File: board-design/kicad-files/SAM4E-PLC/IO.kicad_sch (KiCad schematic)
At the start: 138 parts, among them Q10 BC807, Q11 BC807, Q12 BC807, Q3 BC807, Q4 BC807, Q5 BC807, Q6 BC807, Q7 BC807, Q8 BC807, Q9 BC807, U11 ULN2803CDWR, U12 74AC14SCX, U13 SN74HC240DBR

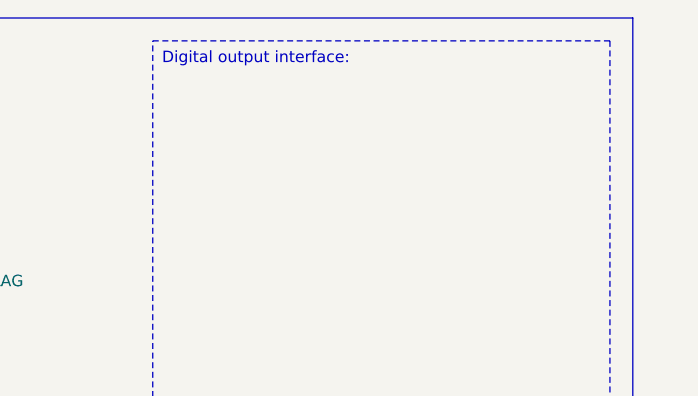
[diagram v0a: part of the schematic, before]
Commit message: [FIX]
Updated footprints for tactile switches.

Signed-off-by: Nicolae-Andrei Vasile <vasilenicolaeandrei@gmail.com>
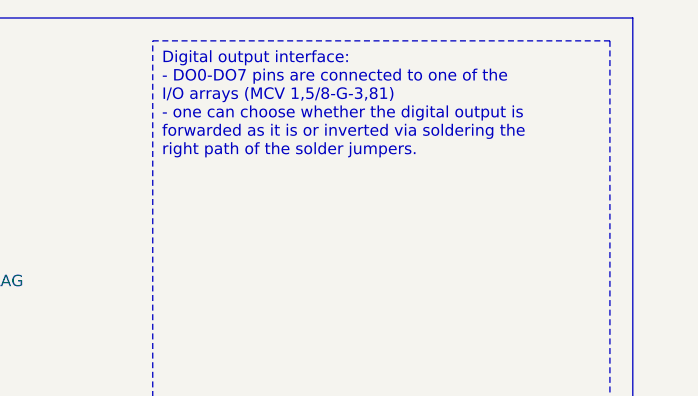
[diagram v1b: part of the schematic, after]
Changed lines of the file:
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@@
     (fill (type none))
   )
-  (text_box "Digital output interface:\n"
+  (text_box "Digital output interface:\n- DO0-DO7 pins are connected to one of the I/O arrays (MCV 1,5/8-G-3,81)\n- one can choose whether the digital output is forwarded as it is or inverted via soldering the right path of the solder jumpers."
     (at 349.25 20.32 0) (size 50.8 40.64)
     (stroke (width 0) (type dash) (color 255 0 0 1))

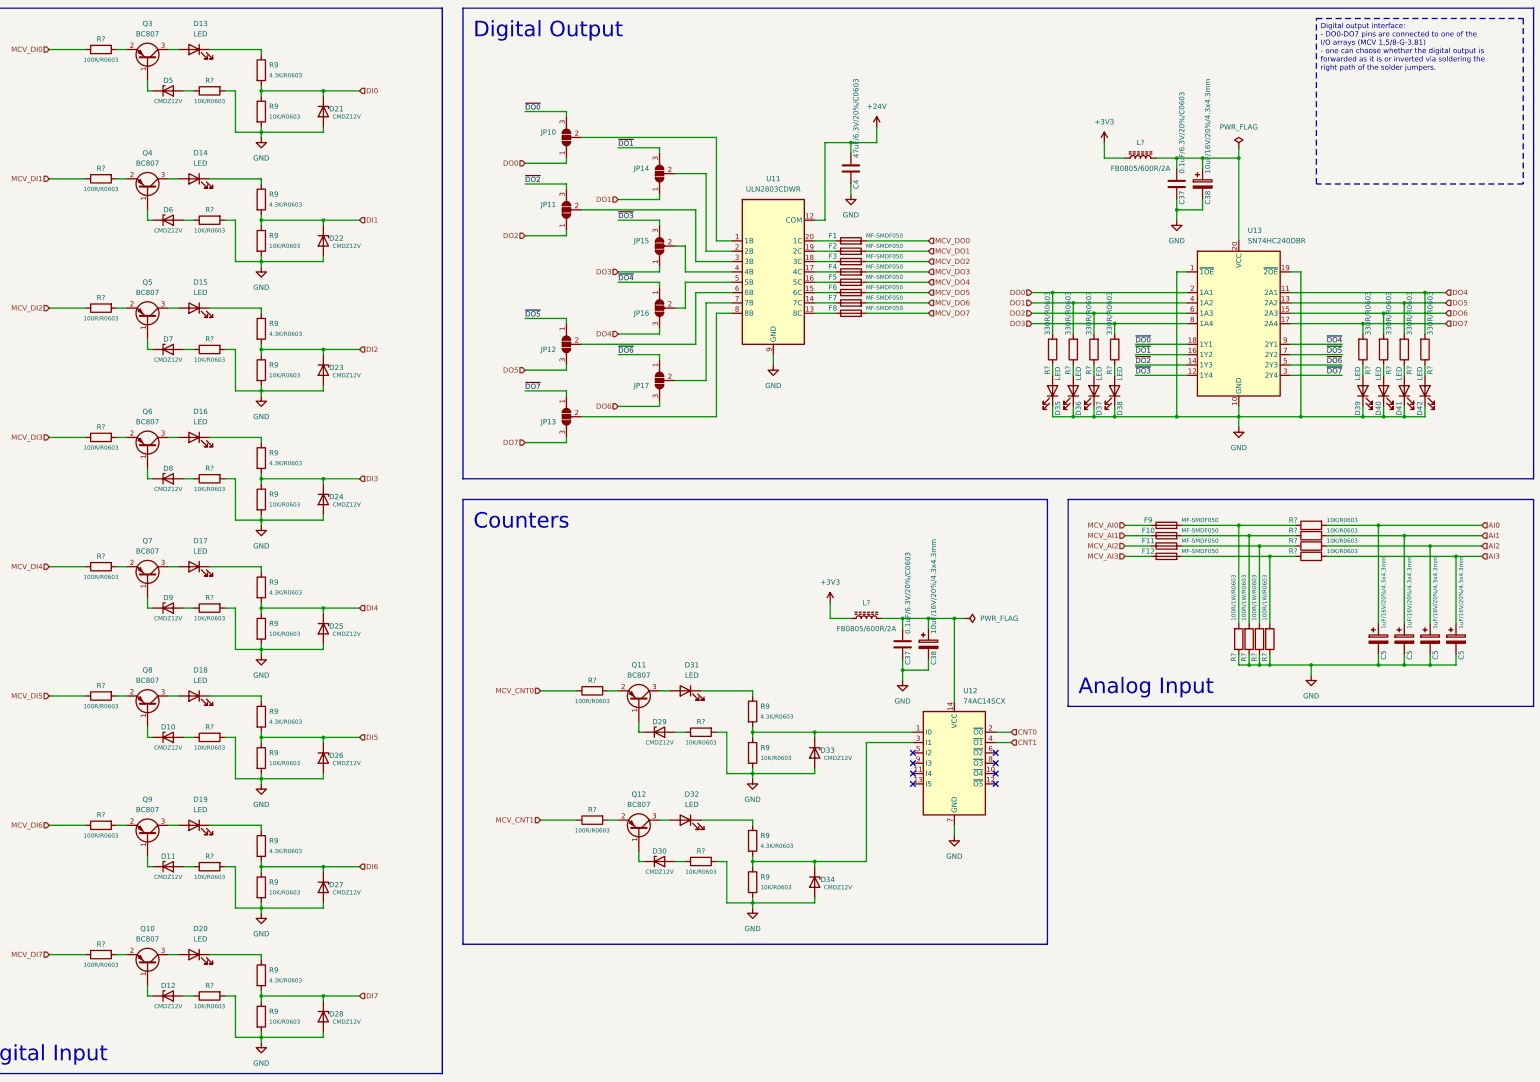
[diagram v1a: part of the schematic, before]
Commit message: [UPDATE]
Refactored schematic for LTE, Power and other schematic sub-sheets.

Signed-off-by: Nicolae-Andrei Vasile <vasilenicolaeandrei@gmail.com>
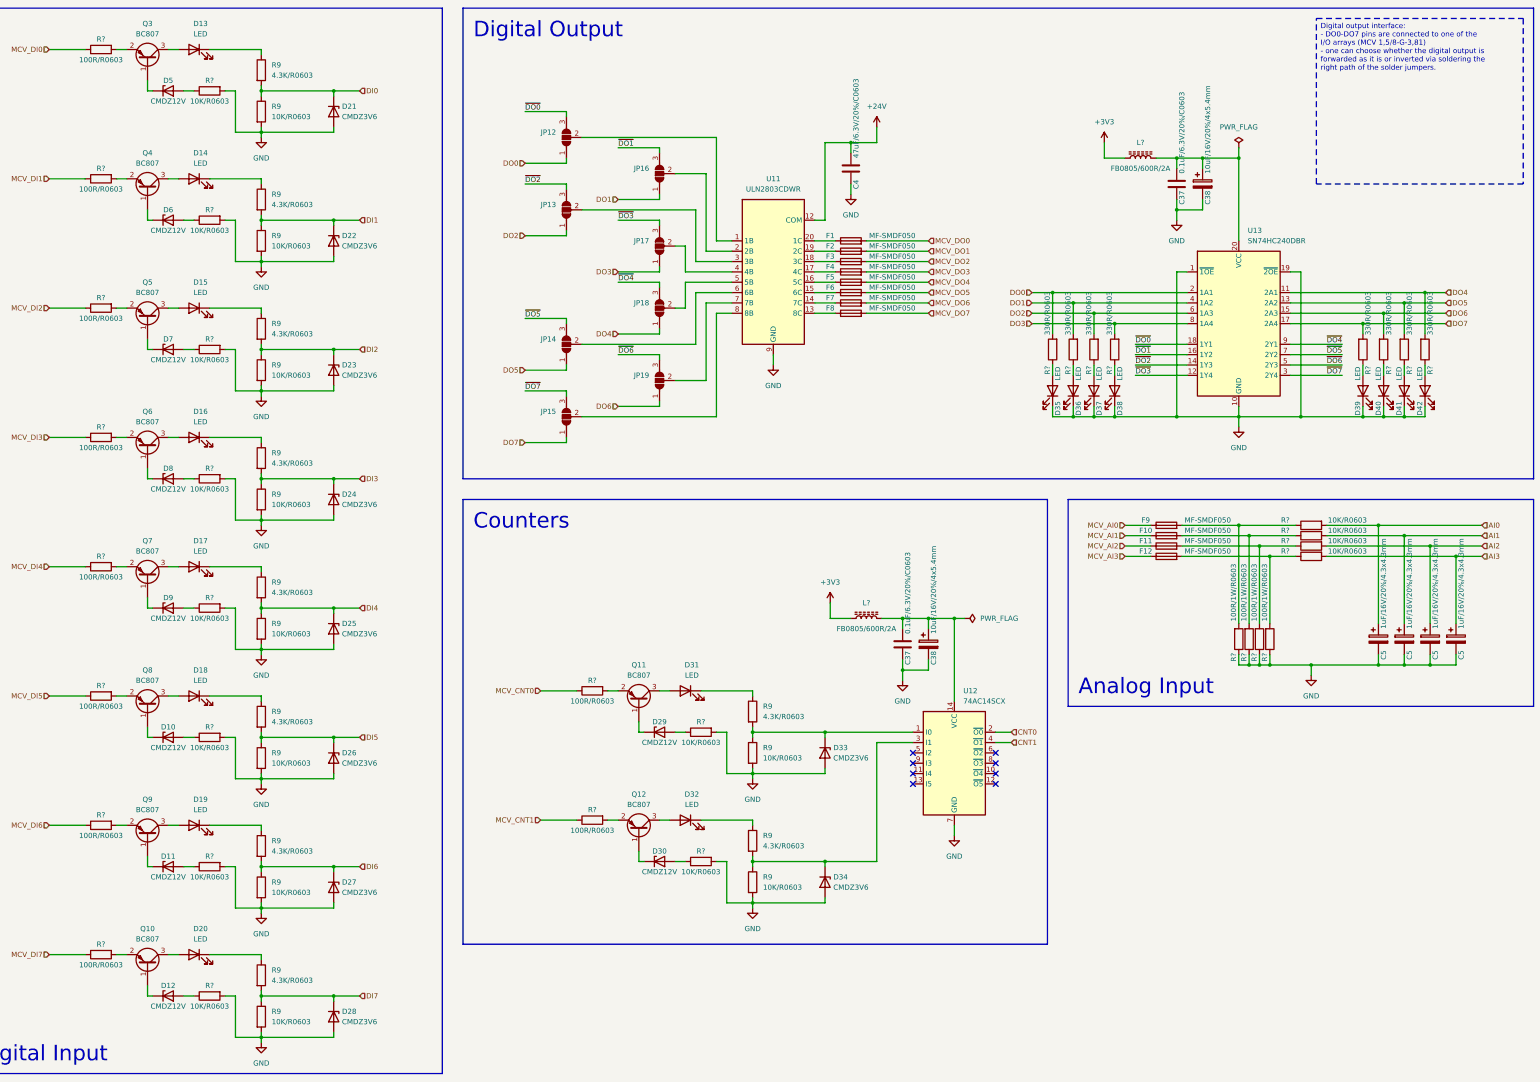
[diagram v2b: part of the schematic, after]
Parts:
- removed C5 (x3): 1uF/16V/20%/4.3x4.3mm, symbol Device:C_Polarized
- removed JP11, JP12: SolderJumper_3_Open, symbol Jumper:SolderJumper_3_Open
- removed L?: FB0805/600R/2A, symbol Device:L_Ferrite
- removed R9 (x9): 10K/R0603, symbol Device:R
- removed R9 (x9): 4.3K/R0603, symbol Device:R
- removed R? (x3): 100R/1W/R0603, Resistor_SMD:R_0603_1608Metric, symbol Device:R
- removed R? (x9): 100R/R0603, Resistor_SMD:R_0603_1608Metric, symbol Device:R
- removed R? (x12): 10K/R0603, Resistor_SMD:R_0603_1608Metric, symbol Device:R
- added C5 (x3): 1uF/16V/20%/4.3x4.3mm, symbol Device:C_Polarized
- added JP18, JP19: SolderJumper_3_Open, Jumper:SolderJumper-3_P1.3mm_Open_Pad1.0x1.5mm, symbol Jumper:SolderJumper_3_Open
- added L?: FB0805/600R/2A, Inductor_SMD:L_0805_2012Metric, symbol Device:L_Ferrite
- added R9 (x9), R? (x12): 10K/R0603, Resistor_SMD:R_0603_1608Metric, symbol Device:R
- added R9 (x9): 4.3K/R0603, Resistor_SMD:R_0603_1608Metric, symbol Device:R
- added R? (x9): 100R/R0603, Resistor_SMD:R_0603_1608Metric, symbol Device:R
- added R? (x3): 100R/1W/R0603, Resistor_SMD:R_0603_1608Metric, symbol Device:R
- C37, C4: footprint (none) -> Capacitor_SMD:C_0603_1608Metric
- C38: value 10uF/16V/20%/4.3x4.3mm -> 10uF/16V/20%/4x5.4mm; footprint (none) -> Capacitor_SMD:CP_Elec_4x5.4
- D10, D11, D12, D29, D30, D5, D6, D7, D8, D9: footprint (none) -> Diode_SMD:D_SOD-323
- D13, D14, D15, D16, D17, D18, D19, D20, D31, D32, D35, D36, D37, D38, D39, D40, D41, D42: footprint (none) -> LED_SMD:LED_0805_2012Metric
- D21, D22, D23, D24, D25, D26, D27, D28, D33, D34: value CMDZ12V -> CMDZ3V6; footprint (none) -> Diode_SMD:D_SOD-323
- F1, F10, F11, F12, F2, F3, F4, F5, F6, F7, F8, F9: footprint (none) -> Fuse:Fuse_2010_5025Metric
- JP12: renamed from JP10; footprint (none) -> Jumper:SolderJumper-3_P1.3mm_Open_Pad1.0x1.5mm
- JP13, JP14, JP15, JP16, JP17: footprint (none) -> Jumper:SolderJumper-3_P1.3mm_Open_Pad1.0x1.5mm
- L?: footprint (none) -> Inductor_SMD:L_0805_2012Metric
- R9: footprint (none) -> Resistor_SMD:R_0603_1608Metric
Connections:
- net +3V3: now also L?.1
- net AI1: now also C5.1, R?.2
- net AI2: now also C5.1, R?.2
- net AI3: now also C5.1, R?.2
- net DI1: now also R9.1, R9.2
- net DI2: now also R9.1, R9.2
- net DI3: now also R9.1, R9.2
- net DI4: now also R9.1, R9.2
- net DI5: now also R9.1, R9.2
- net DI6: now also R9.1, R9.2
- net DI7: now also R9.1, R9.2
- net DO1: now also JP16.1 (A); no longer JP14.1 (A)
- net DO2: now also JP13.1 (A)
- net DO3: now also JP17.1 (A); no longer JP15.1 (A)
- net DO4: now also JP18.1 (A); no longer JP16.3 (B)
- net DO5: now also JP14.1 (A)
- net DO6: now also JP19.1 (A); no longer JP17.3 (B)
- net DO7: now also JP15.1 (A); no longer JP13.3 (B)
- net GND: now also C5.2, C5.2, C5.2, R9.2, R9.2, R9.2, R9.2, R9.2, R9.2, R9.2, R9.2, R9.2, R?.1, R?.1, R?.1, R?.2, R?.2, R?.2, R?.2, R?.2, R?.2, R?.2, R?.2, R?.2
- net MCV_CNT0: now also R?.1
- net MCV_CNT1: now also R?.1
- net MCV_DI1: now also R?.1
- net MCV_DI2: now also R?.1
- net MCV_DI3: now also R?.1
- net MCV_DI4: now also R?.1
- net MCV_DI5: now also R?.1
- net MCV_DI6: now also R?.1
- net MCV_DI7: now also R?.1
- net ~{DO1}: now also JP16.3 (B); no longer JP14.3 (B)
- net ~{DO2}: now also JP13.3 (B)
- net ~{DO3}: now also JP17.3 (B); no longer JP15.3 (B)
- net ~{DO4}: now also JP18.3 (B); no longer JP16.1 (A)
- net ~{DO5}: now also JP14.3 (B)
- net ~{DO6}: now also JP19.3 (B); no longer JP17.1 (A)
- net ~{DO7}: now also JP15.3 (B); no longer JP13.1 (A)
- net at C37.1, C38.1, U12.14 (VCC): now also L?.2
- net at D20.1 (K): now also R9.1
- net at Q8.2 (E): now also R?.2
- net at D8.2 (A): now also R?.1
- net at U11.3 (3B): now also JP13.2 (C)
- net at JP14.2 (C): now also U11.6 (6B); no longer U11.2 (2B)
- net at F11.2: now also R?.1, R?.2
- net at F10.2: now also R?.1, R?.2
- net at D12.2 (A): now also R?.1
- net at Q7.2 (E): now also R?.2
- net at F12.2: now also R?.1, R?.2
- net at Q5.2 (E): now also R?.2
- net at D15.1 (K): now also R9.1
- net at D14.1 (K): now also R9.1
- net at Q6.2 (E): now also R?.2
- net at D33.1 (K), U12.1 (I0): now also R9.1, R9.2
- net at D34.1 (K), U12.3 (I1): now also R9.1, R9.2
- net at Q12.2 (E): now also R?.2
- net at D16.1 (K): now also R9.1
- net at Q4.2 (E): now also R?.2
- net at Q11.2 (E): now also R?.2
- net at D31.1 (K): now also R9.1
- net at D17.1 (K): now also R9.1
- net at D19.1 (K): now also R9.1
- net at D32.1 (K): now also R9.1
- net at D18.1 (K): now also R9.1
- net at D9.2 (A): now also R?.1
- net at D11.2 (A): now also R?.1
- net at D6.2 (A): now also R?.1
- net at JP15.2 (C): now also U11.8 (8B); no longer U11.4 (4B)
- net at U11.5 (5B): now also JP18.2 (C); no longer JP16.2 (C)
- net at U11.7 (7B): now also JP19.2 (C); no longer JP17.2 (C)
- net at D7.2 (A): now also R?.1
- net at D29.2 (A): now also R?.1
- net at D10.2 (A): now also R?.1
- net at D30.2 (A): now also R?.1
- net at Q10.2 (E): now also R?.2
- net at Q9.2 (E): now also R?.2
- new net: JP17.2 (C), U11.4 (4B)
- new net: JP16.2 (C), U11.2 (2B)
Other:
- moved on the sheet: D21

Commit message: [UPDATE]
First draft of SAM4E-PLC schematic completed.

Signed-off-by: Nicolae-Andrei Vasile <vasilenicolaeandrei@gmail.com>
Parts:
- added J? (x4): Screw_Terminal_01x11, Connector_Phoenix_MSTB:PhoenixContact_MSTBVA_2,5_11-G-5,08_1x11_P5.08mm_Vertical, symbol Connector:Screw_Terminal_01x11
- renumbered D11 to D10, D12 to D11, D13 to D12, D14 to D13, D15 to D14, D16 to D15, D17 to D16, D18 to D17, D19 to D18, D20 to D19, D21 to D20, D22 to D21, D23 to D22, D24 to D23, D25 to D24, D26 to D25, D27 to D26, D28 to D27, D29 to D28, D30 to D29, D31 to D30, D32 to D31, D33 to D32, D34 to D33, D35 to D34, D36 to D35, D37 to D36, D38 to D37, D39 to D38, D40 to D39, D5 to D4, D41 to D40, D42 to D41, D6 to D5, D7 to D6, D8 to D7, D9 to D8, D10 to D9
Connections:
- net GND: now also J?.1 (Pin_1), J?.1 (Pin_1), J?.2 (Pin_2), J?.2 (Pin_2)
- net MCV_AI0: now also J?.4 (Pin_4)
- net MCV_AI1: now also J?.5 (Pin_5)
- net MCV_AI2: now also J?.6 (Pin_6)
- net MCV_AI3: now also J?.7 (Pin_7)
- net MCV_CNT0: now also J?.2 (Pin_2)
- net MCV_CNT1: now also J?.3 (Pin_3)
- net MCV_DI0: now also J?.4 (Pin_4)
- net MCV_DI1: now also J?.5 (Pin_5)
- net MCV_DI2: now also J?.6 (Pin_6)
- net MCV_DI3: now also J?.7 (Pin_7)
- net MCV_DI4: now also J?.8 (Pin_8)
- net MCV_DI5: now also J?.9 (Pin_9)
- net MCV_DI6: now also J?.10 (Pin_10)
- net MCV_DI7: now also J?.11 (Pin_11)
- net MCV_DO0: now also J?.4 (Pin_4)
- net MCV_DO1: now also J?.5 (Pin_5)
- net MCV_DO2: now also J?.6 (Pin_6)
- net MCV_DO3: now also J?.7 (Pin_7)
- net MCV_DO4: now also J?.8 (Pin_8)
- net MCV_DO5: now also J?.9 (Pin_9)
- net MCV_DO6: now also J?.10 (Pin_10)
- net MCV_DO7: now also J?.11 (Pin_11)
- new net Earth_Protective: J?.3 (Pin_3), J?.3 (Pin_3)
- new net MCV_CAN0_H: J?.8 (Pin_8)
- new net MCV_CAN0_L: J?.9 (Pin_9)
- new net MCV_CAN1_H: J?.10 (Pin_10)
- new net MCV_CAN1_L: J?.11 (Pin_11)
- new net MCV_RS_A: J?.3 (Pin_3)
- new net MCV_RS_B: J?.2 (Pin_2)
- new net MCV_RTD0_FORCE+: J?.4 (Pin_4)
- new net MCV_RTD0_FORCE-: J?.7 (Pin_7)
- new net MCV_RTD0_RTDIN+: J?.5 (Pin_5)
- new net MCV_RTD0_RTDIN-: J?.6 (Pin_6)
- new net MCV_RTD1_FORCE+: J?.8 (Pin_8)
- new net MCV_RTD1_FORCE-: J?.11 (Pin_11)
- new net MCV_RTD1_RTDIN+: J?.9 (Pin_9)
- new net MCV_RTD1_RTDIN-: J?.10 (Pin_10)
- new net VIN_24V: J?.1 (Pin_1), J?.1 (Pin_1)
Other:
- note added: "I/O"
- moved on the sheet: C37, C38, C4, C5, D28, D29, D30, D31, D32, D33, D34, D35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
